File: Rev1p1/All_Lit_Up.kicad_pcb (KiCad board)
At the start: 2 copper layers, 101.6 x 101.6 mm, 84 parts, among them U1 MCP1640BMC, U2 TLC555xPW

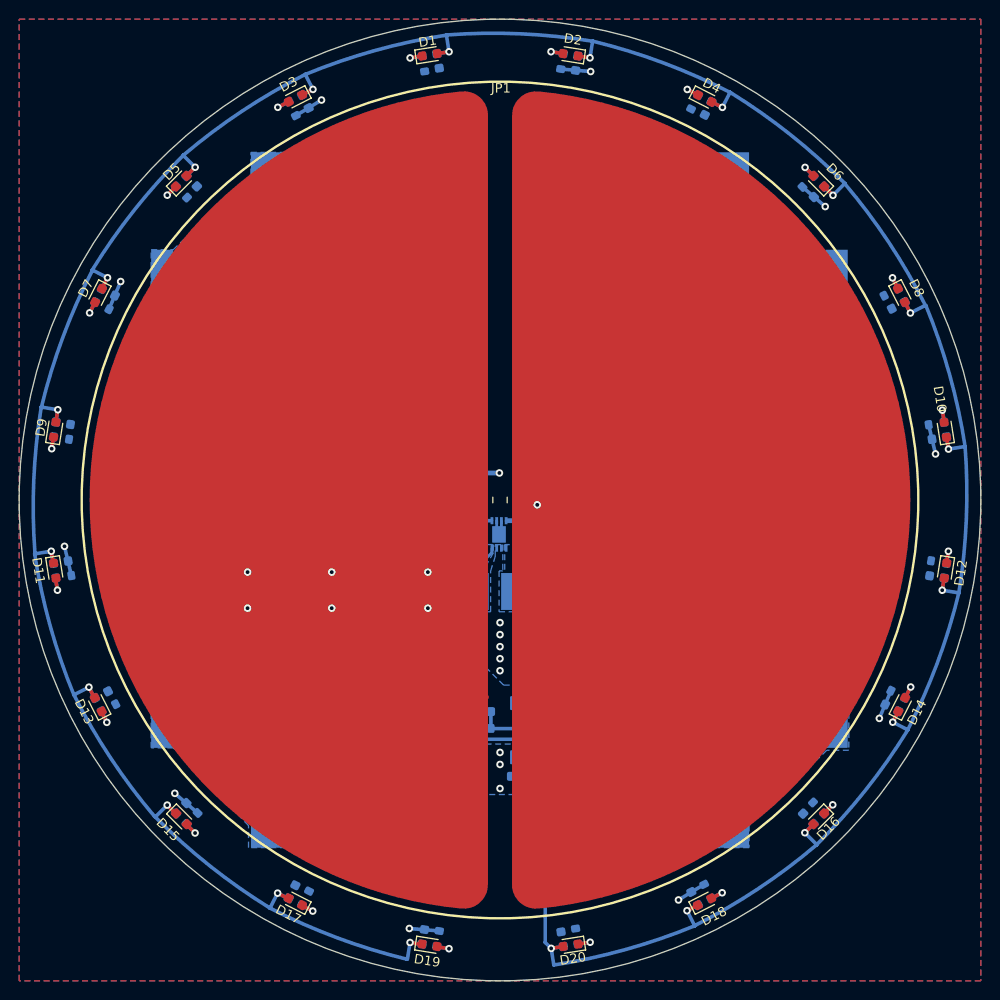
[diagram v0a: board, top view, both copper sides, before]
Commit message: Improved 1p1 Design
Cleaned up design, removed DFN for SOIC. added BOM, Schematic, & Step Files. reduced size to 100mm x 100mm. improved traces & Vias.
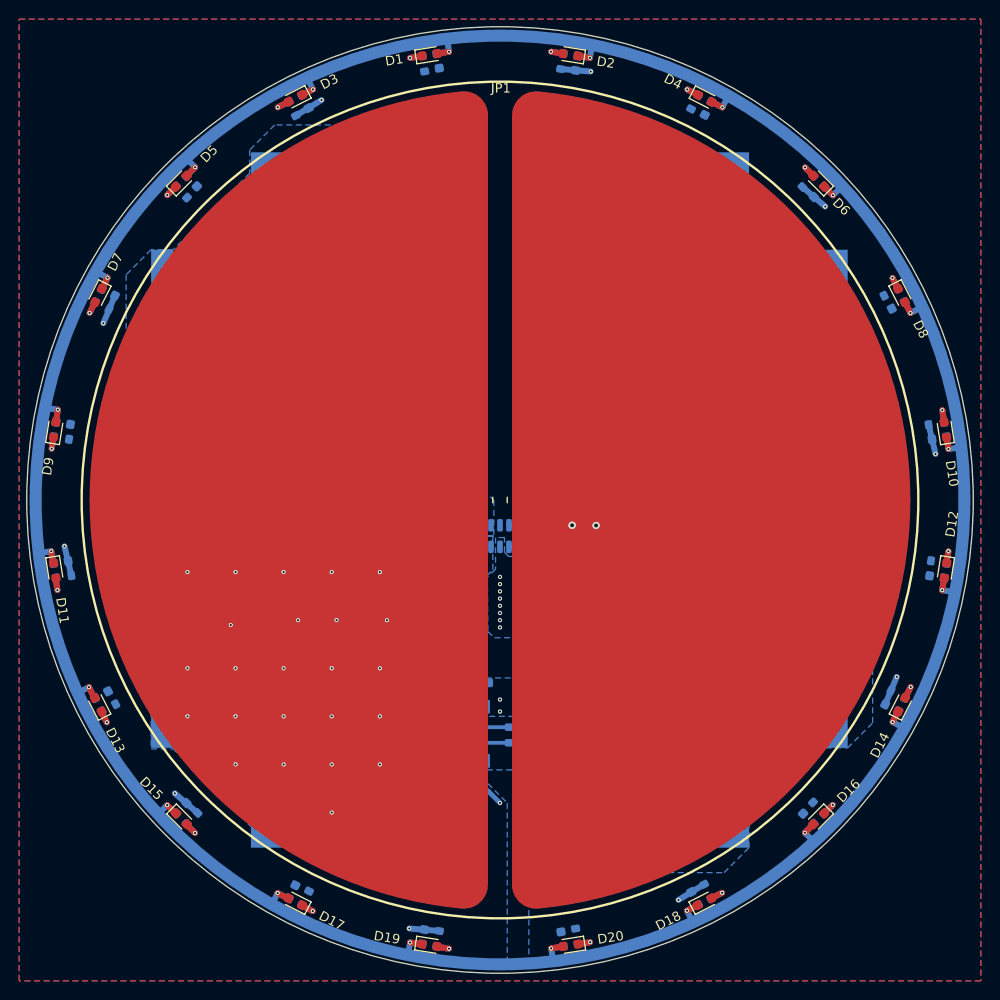
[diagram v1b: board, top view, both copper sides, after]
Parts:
- U1: value MCP1640BMC -> MCP1640Bx-xCHY; footprint Package_DFN_QFN:DFN-8-1EP_3x2mm_P0.5mm_EP1.75x1.45mm -> Package_TO_SOT_SMD:SOT-23-6
- moved G3 35.8 mm to (96.5, 91.4)
- moved R18 14.5 mm to (73.4, 106.9), turned to 180 degrees
- moved C22 14.4 mm to (71.5, 95.2), turned to 90 degrees
- moved C20 11.4 mm to (79.0, 95.5), turned to 0 degrees
- moved R20 10.6 mm to (74.2, 95.5), turned to 0 degrees
- moved R12 10.00 mm to (81.6, 81.1), turned to 0 degrees
- moved R11 9.60 mm to (79.0, 82.0), turned to 90 degrees
- moved C19 8.20 mm to (79.0, 97.8), turned to 0 degrees
- moved L1 7.41 mm to (71.1, 80.0), turned to 90 degrees
- moved C12 7.11 mm to (64.5, 80.0), turned to 90 degrees
- moved U2 6.44 mm to (73.0, 100.9), turned to 90 degrees
- moved C18 6.25 mm to (79.8, 101.9), turned to 0 degrees
- moved C15 4.27 mm to (80.5, 85.9)
- moved C11 3.34 mm to (81.8, 78.1)
- moved R19 2.85 mm to (77.2, 101.0), turned to 90 degrees
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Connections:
- R11 pad 2: /VFB -> /V_{FB}
- R12 pad 1: /VFB -> /V_{FB}
- U1 pad 1: /VFB -> /SWITCHER
- U1 pad 3: GND -> /PWR_EN
- U1 pad 4: /PWR_EN -> /V_{FB}
- U1 pad 5: /SWITCHER -> VCC
- U1 pad 6: VCC -> V_{BAT}
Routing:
- net /LED_SET: track 409.0 -> 77.8 mm
- net V_{BAT}: track 103.5 -> 0.00 mm, vias 6 -> 24
- net /VFB: track 4.69 -> 0.00 mm
- net /PWR_EN: track 4.86 -> 9.21 mm, vias 1 -> 2
- net /V_{FB}: track 0.00 -> 3.62 mm
- net GND: track 3.12 -> 0.00 mm
- net VCC: track 36.1 -> 34.2 mm, vias 19 -> 21
- net /DISCHARGE: track 9.61 -> 7.93 mm
- net /~{RESET}: track 3.30 -> 4.37 mm
- added copper zone on B.Cu, net /LED_SET
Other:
- board size 101.6 x 101.6 mm -> 100 x 100 mm

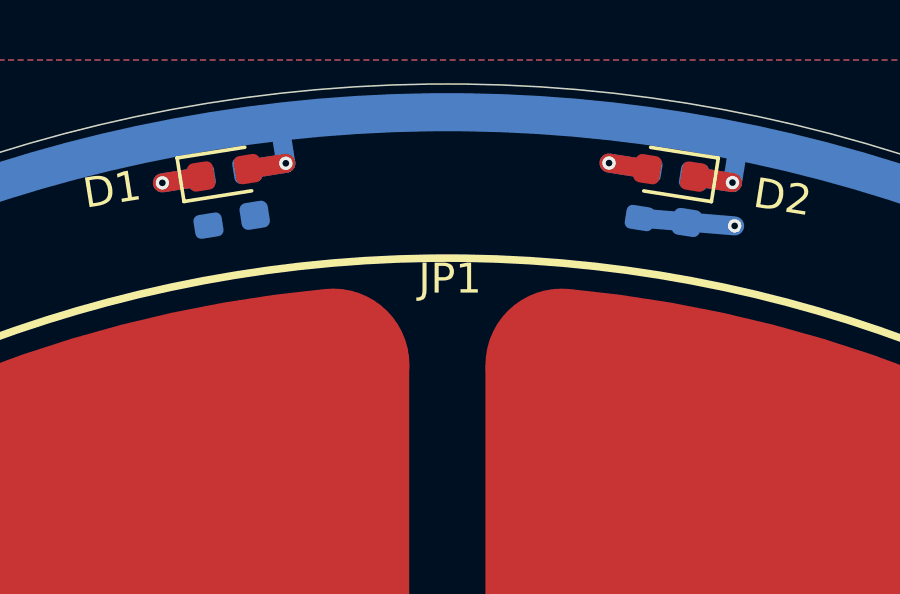
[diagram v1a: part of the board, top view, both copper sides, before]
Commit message: Update to working model
Change LEDs to used Value, Correct to 1k, change resistor values to used. Add LED choice and orientation with silk. correct silk for 1 LED Cap combo. update gbrs. update output documents. Added iBOM
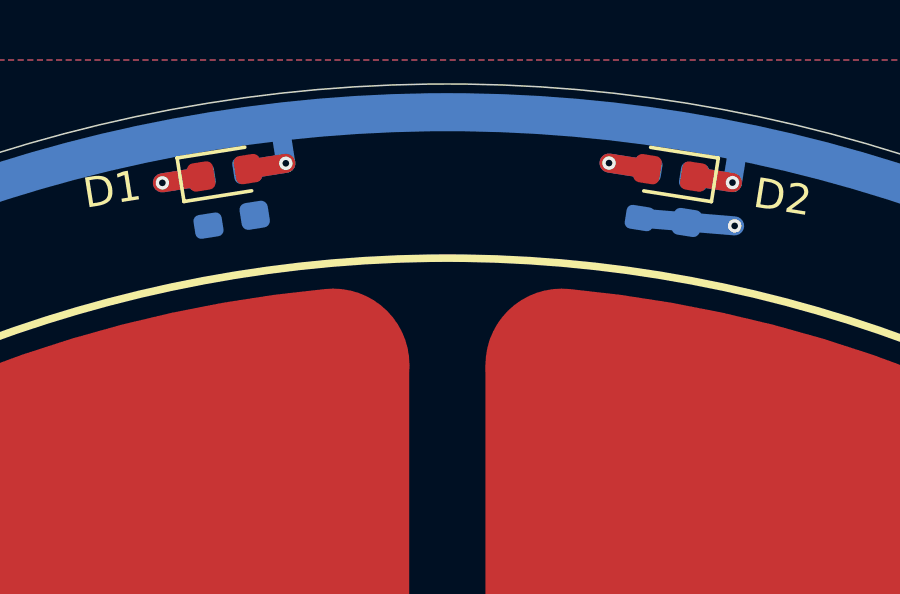
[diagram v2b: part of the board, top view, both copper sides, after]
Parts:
- R1, R15, R16, R22, R23, R26, R4, R5, R8, R9: value 160 -> 120
- R10, R14, R17, R2, R21, R24, R25, R3, R6, R7: value 60.4 -> 56
- R20: value 0 -> 1k
- moved G3 5.43 mm to (95.5, 86.1)
- moved G1 1.53 mm to (76.2, 56.4)
- moved G2 1.49 mm to (72.6, 68.1)
